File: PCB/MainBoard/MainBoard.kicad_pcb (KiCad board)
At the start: 2 copper layers, 100 x 100 mm, 73 parts, among them J1 5442170, J10 Conn_01x06_Socket, J11 Conn_01x06_Socket, J12 Conn_01x04_Socket, J14 Conn_01x03_Socket, J18 Conn_01x04_Socket, J19 Conn_01x04_Socket, J2 5442170, J20 Conn_01x04_Socket, J3 5442170, J4 5442170, J5 Conn_01x03_Socket, J6 Conn_01x03_Socket, J7 Conn_01x03_Socket, J8 5442170, SW1 SW_Push, U1 TPS56339DDC, U2 TPS56339DDC, U3 STM32F103C8Tx, U4 CD74HC00_N_14, U5 TPS56339DDC, U6 CD74HC00_N_14

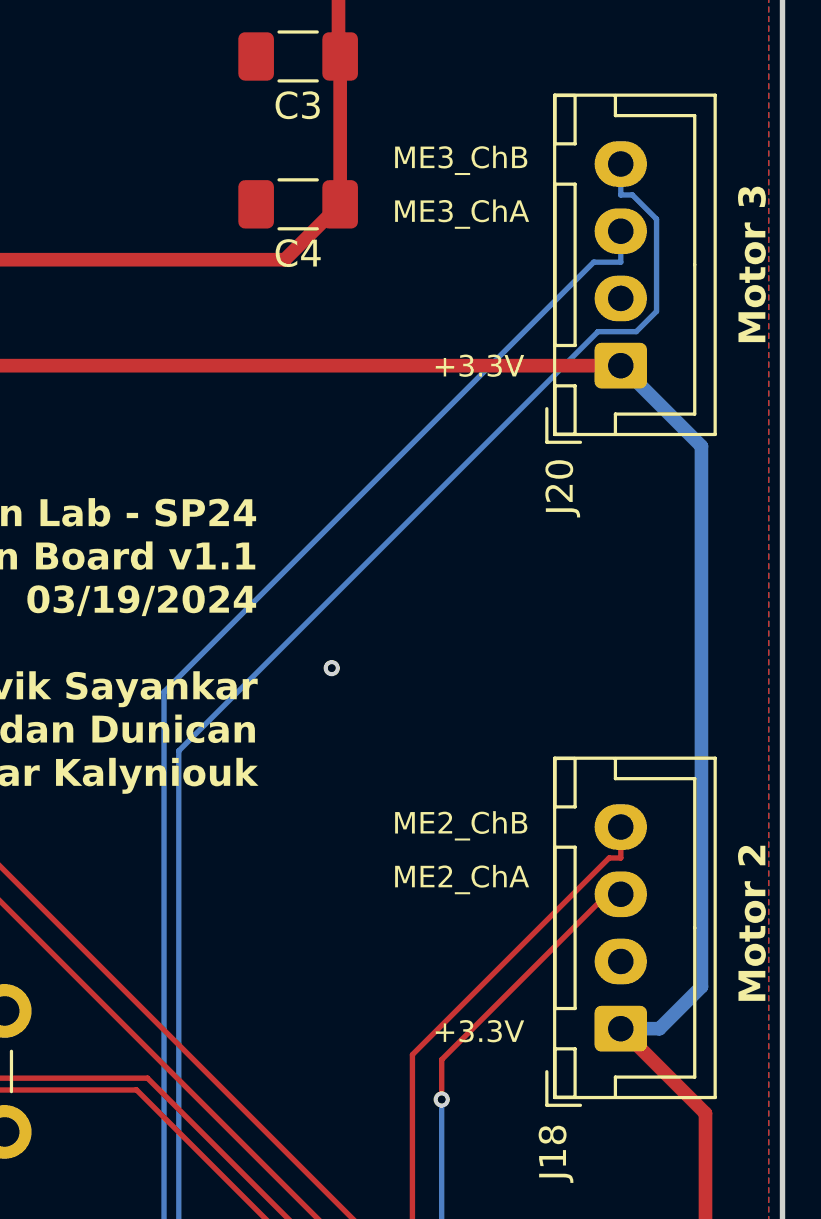
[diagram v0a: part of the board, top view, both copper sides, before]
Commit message: fixing some right angles in board
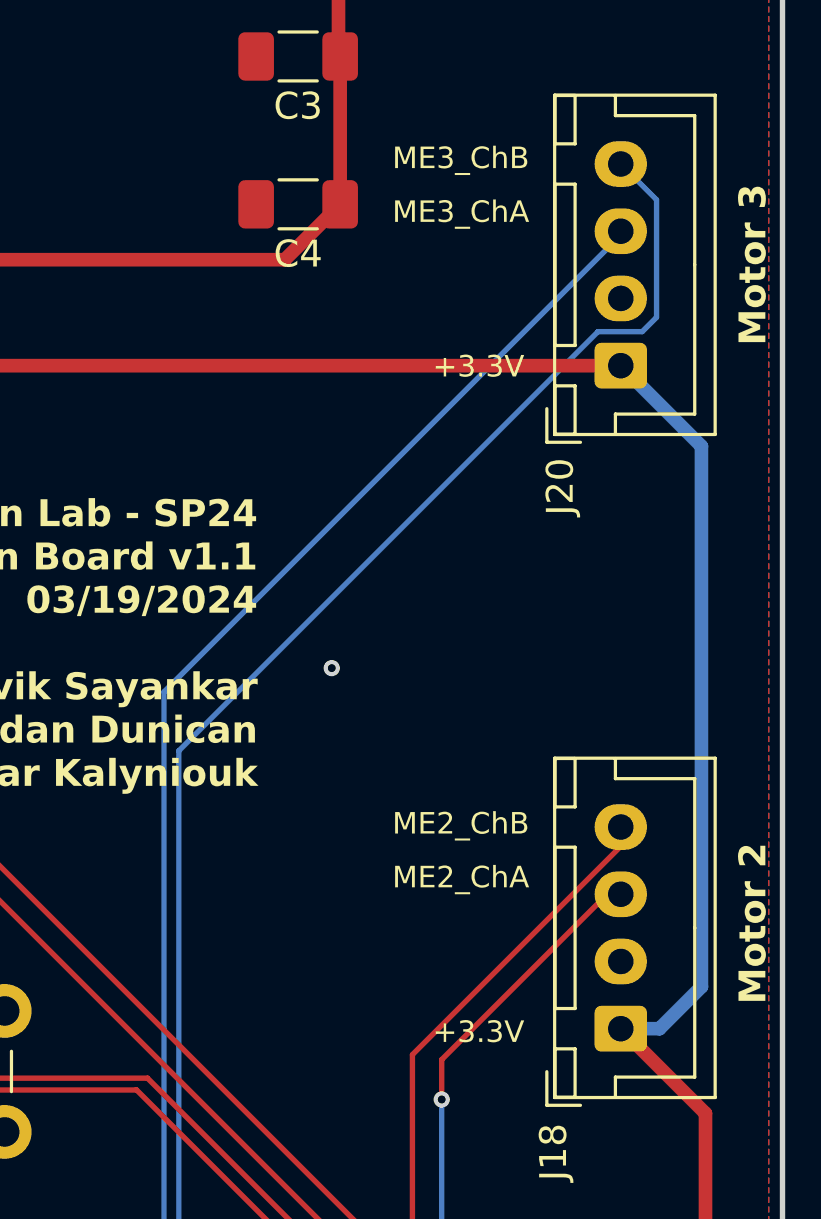
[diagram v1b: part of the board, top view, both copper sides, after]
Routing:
- net /ME3_ChA: track 55.6 -> 55.0 mm
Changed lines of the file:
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@@
+	)
+	(segment
+		(start 188.7513 112.0487)
+		(end 185.5887 115.2113)
+		(width 0.2)
+		(layer "F.Cu")
+		(net 30)
 	)
 	(segment
@@
 	)
 	(segment
+		(start 185.5887 115.2113)
+		(end 180.7613 115.2113)
+		(width 0.2)
+		(layer "F.Cu")
+		(net 30)
+	)
+	(segment
+		(start 188.7513 96.1275)
+		(end 188.7513 112.0487)
+		(width 0.2)
+		(layer "F.Cu")
+		(net 30)
+	)
+	(segment
 		(start 180.3375 114.7875)
 		(end 180.3375 113.1625)
@@
 	)
 	(segment
-		(start 196.0687 88.8101)
+		(start 196.5 87.66)
+		(end 196.5 88.3788)
+		(width 0.2)
+		(layer "F.Cu")
+		(net 30)
+	)
+	(segment
+		(start 196.5 88.3788)
 		(end 188.7513 96.1275)
-		(width 0.2)
-		(layer "F.Cu")
-		(net 30)
-	)
-	(segment
-		(start 188.7513 112.0487)
-		(end 185.5887 115.2113)
-		(width 0.2)
-		(layer "F.Cu")
-		(net 30)
-	)
-	(segment
-		(start 188.7513 96.1275)
-		(end 188.7513 112.0487)
-		(width 0.2)
-		(layer "F.Cu")
-		(net 30)
-	)
-	(segment
-		(start 196.5 87.66)
-		(end 196.5 88.8101)
-		(width 0.2)
-		(layer "F.Cu")
-		(net 30)
-	)
-	(segment
-		(start 185.5887 115.2113)
-		(end 180.7613 115.2113)
-		(width 0.2)
-		(layer "F.Cu")
-		(net 30)
-	)
-	(segment
-		(start 196.5 88.8101)
-		(end 196.0687 88.8101)
 		(width 0.2)
 		(layer "F.Cu")
@@
 	)
 	(segment
-		(start 195.4937 66.6501)
-		(end 179.5113 82.6325)
+		(start 179.5113 110.621)
+		(end 178.8434 111.2889)
+		(width 0.2)
+		(layer "B.Cu")
+		(net 33)
+	)
+	(segment
+		(start 179.5113 82.6325)
+		(end 179.5113 110.621)
 		(width 0.2)
 		(layer "B.Cu")
@@
 	(segment
 		(start 196.5 65.5)
-		(end 196.5 66.6501)
+		(end 196.5 65.6438)
+		(width 0.2)
+		(layer "B.Cu")
+		(net 33)
+	)
+	(segment
+		(start 178.8434 111.2889)
+		(end 178.8434 111.7196)
 		(width 0.2)
 		(layer "B.Cu")
@@
 	)
 	(segment
-		(start 179.5113 82.6325)
-		(end 179.5113 110.621)
-		(width 0.2)
-		(layer "B.Cu")
-		(net 33)
-	)
-	(segment
-		(start 179.5113 110.621)
-		(end 178.8434 111.2889)
-		(width 0.2)
-		(layer "B.Cu")
-		(net 33)
-	)
-	(segment
-		(start 178.8434 111.2889)
-		(end 178.8434 111.7196)
-		(width 0.2)
-		(layer "B.Cu")
-		(net 33)
-	)
-	(segment
-		(start 196.5 66.6501)
-		(end 195.4937 66.6501)
+		(start 196.5 65.6438)
+		(end 179.5113 82.6325)
 		(width 0.2)
 		(layer "B.Cu")
@@
 	)
 	(segment
-		(start 197.8292 68.4832)
-		(end 197.0777 69.2347)
+		(start 197.2965 69.2347)
+		(end 195.6535 69.2347)
+		(width 0.2)
+		(layer "B.Cu")
+		(net 34)
+	)
+	(segment
+		(start 180.0623 84.8259)
+		(end 180.0623 110.9186)
 		(width 0.2)
 		(layer "B.Cu")
@@
 	(segment
 		(start 196.5 63)
-		(end 196.5 64.1501)
+		(end 197.8292 64.3292)
 		(width 0.2)
 		(layer "B.Cu")
@@
 	)
 	(segment
-		(start 196.5 64.1501)
-		(end 196.9313 64.1501)
+		(start 197.8292 64.3292)
+		(end 197.8292 68.702)
 		(width 0.2)
 		(layer "B.Cu")
@@
 	)
 	(segment
-		(start 197.8292 65.048)
-		(end 197.8292 68.4832)
-		(width 0.2)
-		(layer "B.Cu")
-		(net 34)
-	)
-	(segment
-		(start 197.0777 69.2347)
-		(end 195.6535 69.2347)
-		(width 0.2)
-		(layer "B.Cu")
-		(net 34)
-	)
-	(segment
-		(start 196.9313 64.1501)
-		(end 197.8292 65.048)
-		(width 0.2)
-		(layer "B.Cu")
-		(net 34)
-	)
-	(segment
-		(start 180.0623 84.8259)
-		(end 180.0623 110.9186)
-		(width 0.2)
-		(layer "B.Cu")
+		(start 197.8292 68.702)
+		(end 197.2965 69.2347)
+		(width 0.2)
+		(layer "B.Cu")

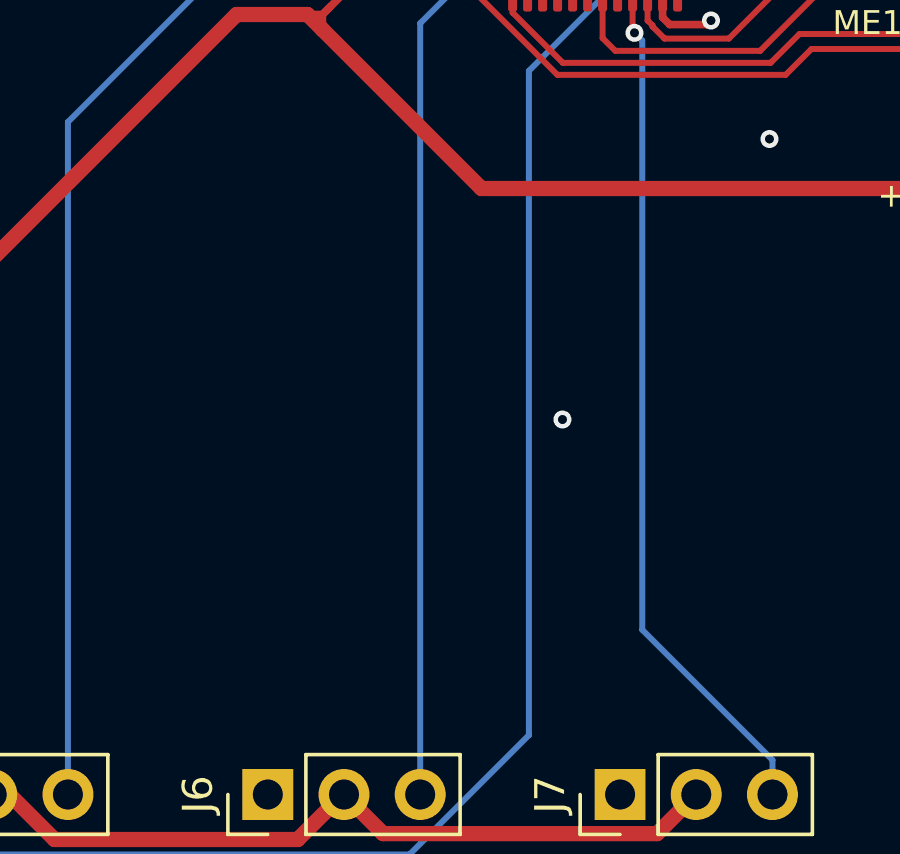
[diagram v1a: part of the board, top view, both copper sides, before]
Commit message: v1.1 of MainBoard complete - PCBWay DRC Passes
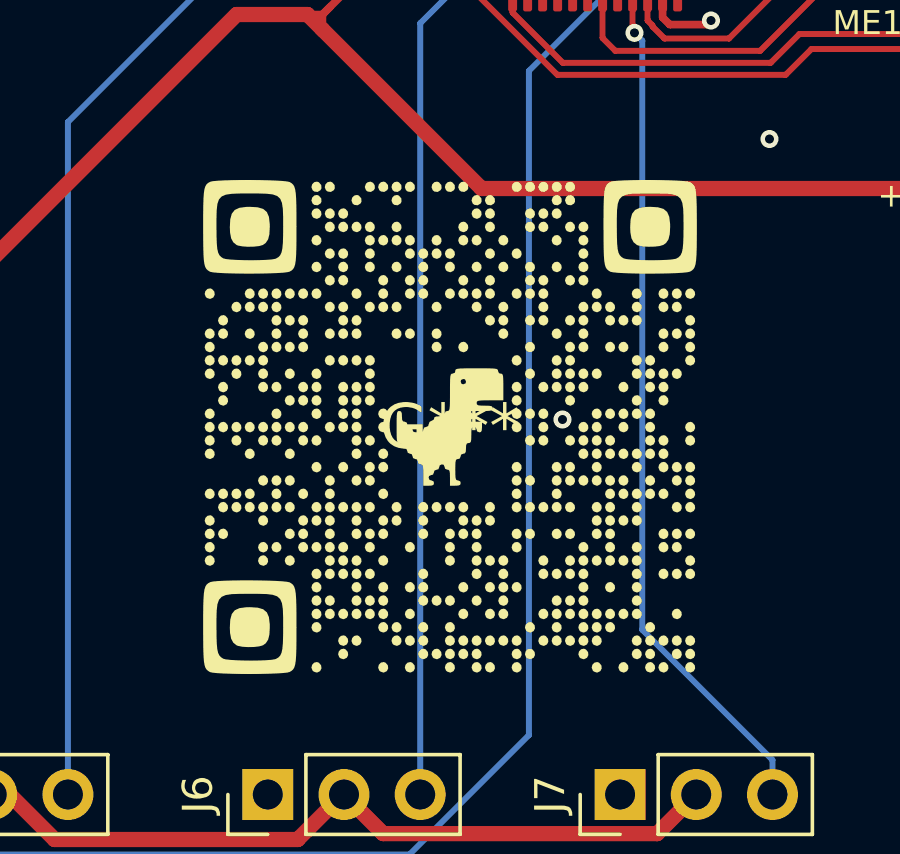
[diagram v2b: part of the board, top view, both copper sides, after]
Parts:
- added G***: LOGO, LOGO, F.Cu at (175.2, 127.8)
